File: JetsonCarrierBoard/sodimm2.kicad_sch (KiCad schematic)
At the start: 1 part

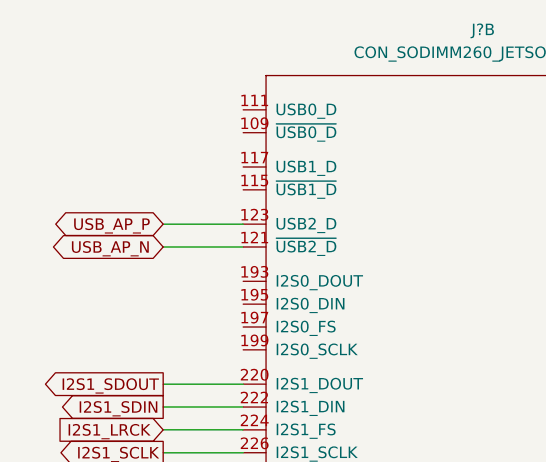
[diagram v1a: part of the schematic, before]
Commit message: Finished USB-C w/ Alt mode and PD Wiring V1
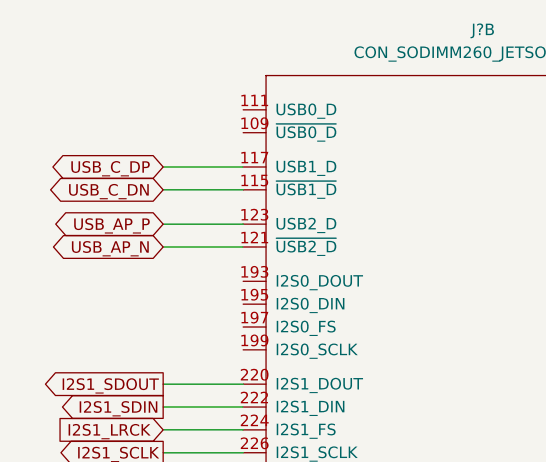
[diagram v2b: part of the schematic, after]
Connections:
- net USB_C_DN: now reaches J?.115 (~{USB1_D})
- net USB_C_DP: now reaches J?.117 (USB1_D)
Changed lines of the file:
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@@
+    (stroke (width 0) (type default) (color 0 0 0 0))
+  )
+  (wire (pts (xy 107.95 36.83) (xy 116.84 36.83))
+    (stroke (width 0) (type default) (color 0 0 0 0))
+  )
+  (wire (pts (xy 107.95 34.29) (xy 116.84 34.29))
     (stroke (width 0) (type default) (color 0 0 0 0))
   )
@@
     )
   )
+  (global_label "USB_C_DN" (shape bidirectional) (at 107.95 36.83 180) (fields_autoplaced)
+    (effects (font (size 1.27 1.27)) (justify right))
+    (property "Intersheet References" "${INTERSHEET_REFS}" (id 0) (at 95.9212 36.7506 0)
+      (effects (font (size 1.27 1.27)) (justify right) hide)
+    )
+  )
   (global_label "I2S1_SDIN" (shape output) (at 107.95 60.96 180) (fields_autoplaced)
     (effects (font (size 1.27 1.27)) (justify right))
@@
       (effects (font (size 1.27 1.27)) (justify right) hide)
     )
+  )
+  (global_label "USB_C_DP" (shape bidirectional) (at 107.95 34.29 180) (fields_autoplaced)
+    (effects (font (size 1.27 1.27)) (justify right))
+    (property "Intersheet References" "${INTERSHEET_REFS}" (id 0) (at 95.9817 34.2106 0)
+      (effects (font (size 1.27 1.27)) (justify right) hide)
+    )

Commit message: Small changes
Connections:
- net MIC_SD: now reaches J?.195 (I2S0_DIN)
- net MIC_WS: now reaches J?.197 (I2S0_FS)
- net MIC_SCK: now reaches J?.199 (I2S0_SCLK)
- no-connect marks 16 -> 17
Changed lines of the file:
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@@
   (no_connect (at 116.84 78.74))
   (no_connect (at 116.84 81.28))
+  (no_connect (at 116.84 46.99))
   (wire (pts (xy 107.95 63.5) (xy 116.84 63.5))
+    (stroke (width 0) (type default) (color 0 0 0 0))
+  )
+  (wire (pts (xy 107.95 52.07) (xy 116.84 52.07))
     (stroke (width 0) (type default) (color 0 0 0 0))
   )
@@
   )
   (wire (pts (xy 107.95 34.29) (xy 116.84 34.29))
+    (stroke (width 0) (type default) (color 0 0 0 0))
+  )
+  (wire (pts (xy 107.95 49.53) (xy 116.84 49.53))
     (stroke (width 0) (type default) (color 0 0 0 0))
   )
@@
   )
   (wire (pts (xy 107.95 40.64) (xy 116.84 40.64))
+    (stroke (width 0) (type default) (color 0 0 0 0))
+  )
+  (wire (pts (xy 107.95 54.61) (xy 116.84 54.61))
     (stroke (width 0) (type default) (color 0 0 0 0))
   )
@@
     )
   )
+  (global_label "MIC_SCK" (shape output) (at 107.95 54.61 180) (fields_autoplaced)
+    (effects (font (size 1.27 1.27)) (justify right))
+    (property "Intersheet References" "${INTERSHEET_REFS}" (id 0) (at 97.4936 54.5306 0)
+      (effects (font (size 1.27 1.27)) (justify right) hide)
+    )
+  )
   (global_label "I2S1_SDIN" (shape output) (at 107.95 60.96 180) (fields_autoplaced)
     (effects (font (size 1.27 1.27)) (justify right))
@@
       (effects (font (size 1.27 1.27)) (justify right) hide)
     )
+  )
+  (global_label "MIC_WS" (shape input) (at 107.95 52.07 180) (fields_autoplaced)
+    (effects (font (size 1.27 1.27)) (justify right))
+    (property "Intersheet References" "${INTERSHEET_REFS}" (id 0) (at 98.5821 52.1494 0)
+      (effects (font (size 1.27 1.27)) (justify right) hide)
+    )
+  )
+  (global_label "MIC_SD" (shape output) (at 107.95 49.53 180) (fields_autoplaced)
+    (effects (font (size 1.27 1.27)) (justify right))
+    (property "Intersheet References" "${INTERSHEET_REFS}" (id 0) (at 98.7636 49.4506 0)
+      (effects (font (size 1.27 1.27)) (justify right) hide)
+    )

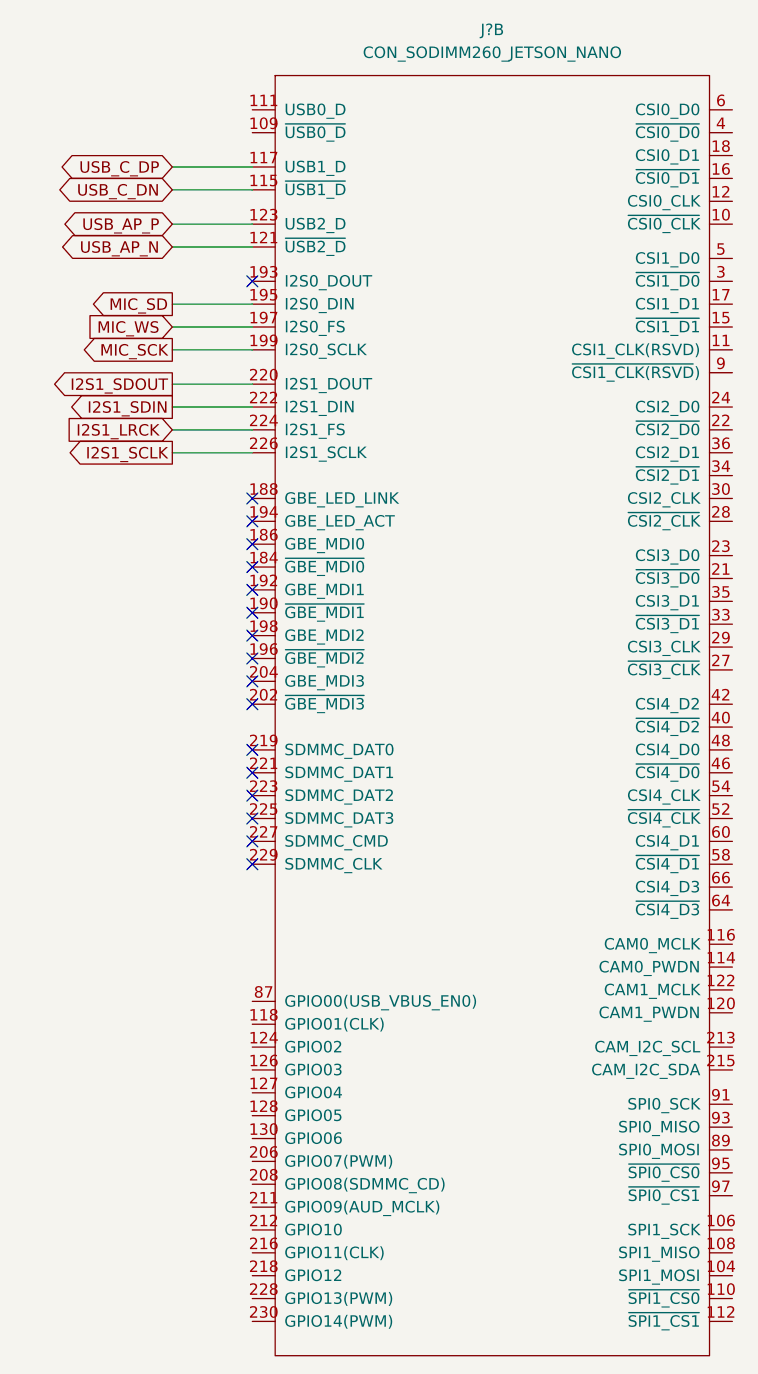
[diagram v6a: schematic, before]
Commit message: Micro USB B 2.0 Basic Wiring
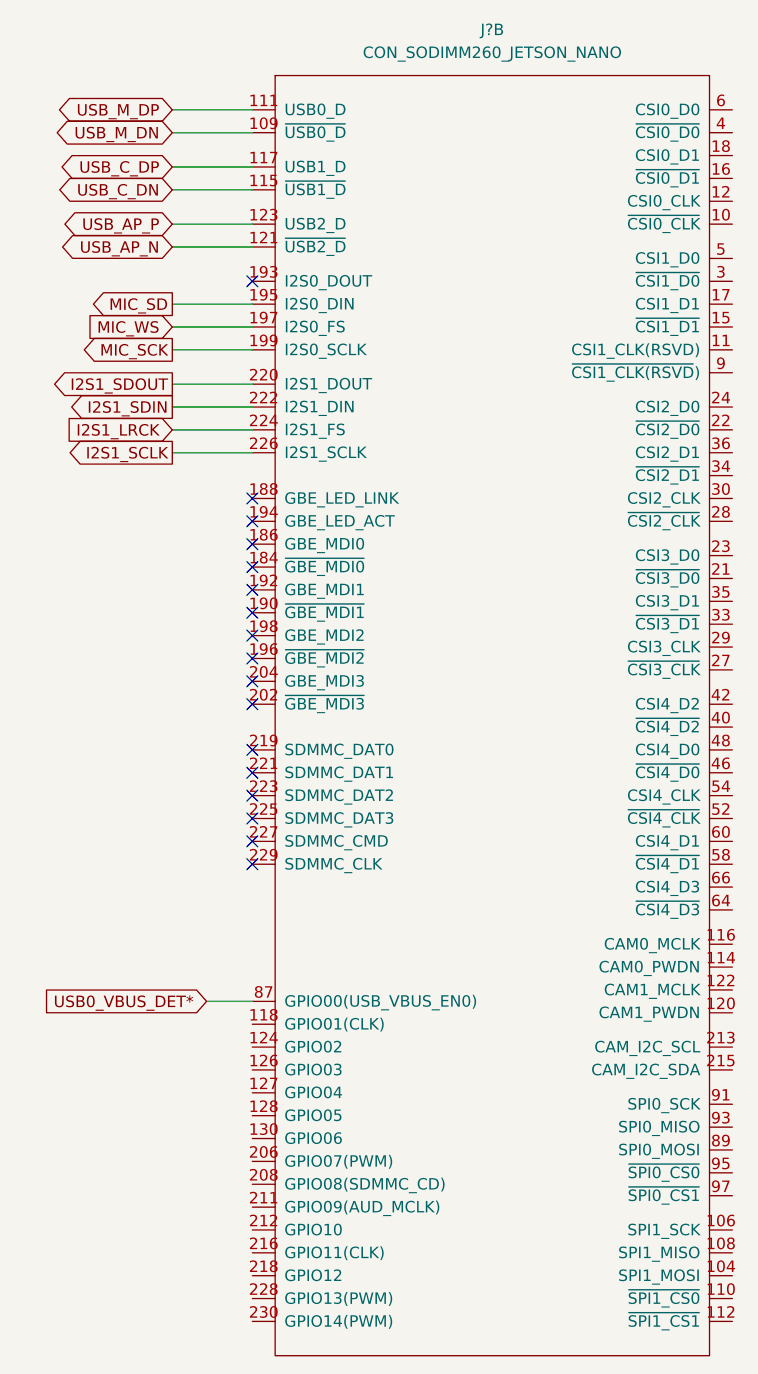
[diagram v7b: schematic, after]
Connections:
- net USB_M_DN: now reaches J?.109 (~{USB0_D})
- net USB_M_DP: now reaches J?.111 (USB0_D)
- net USB0_VBUS_DET*: now reaches J?.87 (GPIO00(USB_VBUS_EN0))
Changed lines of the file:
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@@
   (no_connect (at 116.84 81.28))
   (no_connect (at 116.84 46.99))
+  (wire (pts (xy 107.95 30.48) (xy 116.84 30.48))
+    (stroke (width 0) (type default) (color 0 0 0 0))
+  )
   (wire (pts (xy 107.95 63.5) (xy 116.84 63.5))
     (stroke (width 0) (type default) (color 0 0 0 0))
@@
   )
   (wire (pts (xy 107.95 36.83) (xy 116.84 36.83))
+    (stroke (width 0) (type default) (color 0 0 0 0))
+  )
+  (wire (pts (xy 107.95 27.94) (xy 116.84 27.94))
     (stroke (width 0) (type default) (color 0 0 0 0))
   )
@@
   )
   (wire (pts (xy 107.95 40.64) (xy 116.84 40.64))
+    (stroke (width 0) (type default) (color 0 0 0 0))
+  )
+  (wire (pts (xy 111.76 127) (xy 116.84 127))
     (stroke (width 0) (type default) (color 0 0 0 0))
   )
@@
     (effects (font (size 1.27 1.27)) (justify right))
     (property "Intersheet References" "${INTERSHEET_REFS}" (id 0) (at 95.9212 36.7506 0)
+      (effects (font (size 1.27 1.27)) (justify right) hide)
+    )
+  )
+  (global_label "USB_M_DP" (shape bidirectional) (at 107.95 27.94 180) (fields_autoplaced)
+    (effects (font (size 1.27 1.27)) (justify right))
+    (property "Intersheet References" "${INTERSHEET_REFS}" (id 0) (at 95.8002 27.8606 0)
       (effects (font (size 1.27 1.27)) (justify right) hide)
     )
@@
       (effects (font (size 1.27 1.27)) (justify right) hide)
     )
+  )
+  (global_label "USB0_VBUS_DET*" (shape input) (at 111.76 127 180) (fields_autoplaced)
+    (effects (font (size 1.27 1.27)) (justify right))
+    (property "Intersheet References" "${INTERSHEET_REFS}" (id 0) (at 93.1393 126.9206 0)
+      (effects (font (size 1.27 1.27)) (justify right) hide)
+    )
+  )
+  (global_label "USB_M_DN" (shape bidirectional) (at 107.95 30.48 180) (fields_autoplaced)
+    (effects (font (size 1.27 1.27)) (justify right))
+    (property "Intersheet References" "${INTERSHEET_REFS}" (id 0) (at 95.7398 30.4006 0)
+      (effects (font (size 1.27 1.27)) (justify right) hide)
+    )

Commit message: Connections
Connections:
- net FAN_TACH: now reaches J?.208 (GPIO08(SDMMC_CD))
- net FAN_PWM: now reaches J?.230 (GPIO14(PWM))
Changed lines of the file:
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@@
+    (stroke (width 0) (type default) (color 0 0 0 0))
+  )
+  (wire (pts (xy 111.76 162.56) (xy 116.84 162.56))
     (stroke (width 0) (type default) (color 0 0 0 0))
   )
@@
   )
   (wire (pts (xy 111.76 127) (xy 116.84 127))
+    (stroke (width 0) (type default) (color 0 0 0 0))
+  )
+  (wire (pts (xy 111.76 147.32) (xy 116.84 147.32))
     (stroke (width 0) (type default) (color 0 0 0 0))
   )
@@
     )
   )
+  (global_label "FAN_PWM" (shape output) (at 111.76 162.56 180) (fields_autoplaced)
+    (effects (font (size 1.27 1.27)) (justify right))
+    (property "Intersheet References" "${INTERSHEET_REFS}" (id 0) (at 100.6988 162.4806 0)
+      (effects (font (size 1.27 1.27)) (justify right) hide)
+    )
+  )
   (global_label "MIC_WS" (shape input) (at 107.95 52.07 180) (fields_autoplaced)
     (effects (font (size 1.27 1.27)) (justify right))
@@
       (effects (font (size 1.27 1.27)) (justify right) hide)
     )
+  )
+  (global_label "FAN_TACH" (shape input) (at 111.76 147.32 180) (fields_autoplaced)
+    (effects (font (size 1.27 1.27)) (justify right))
+    (property "Intersheet References" "${INTERSHEET_REFS}" (id 0) (at 100.215 147.2406 0)
+      (effects (font (size 1.27 1.27)) (justify right) hide)
+    )
